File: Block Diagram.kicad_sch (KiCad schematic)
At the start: 0 parts

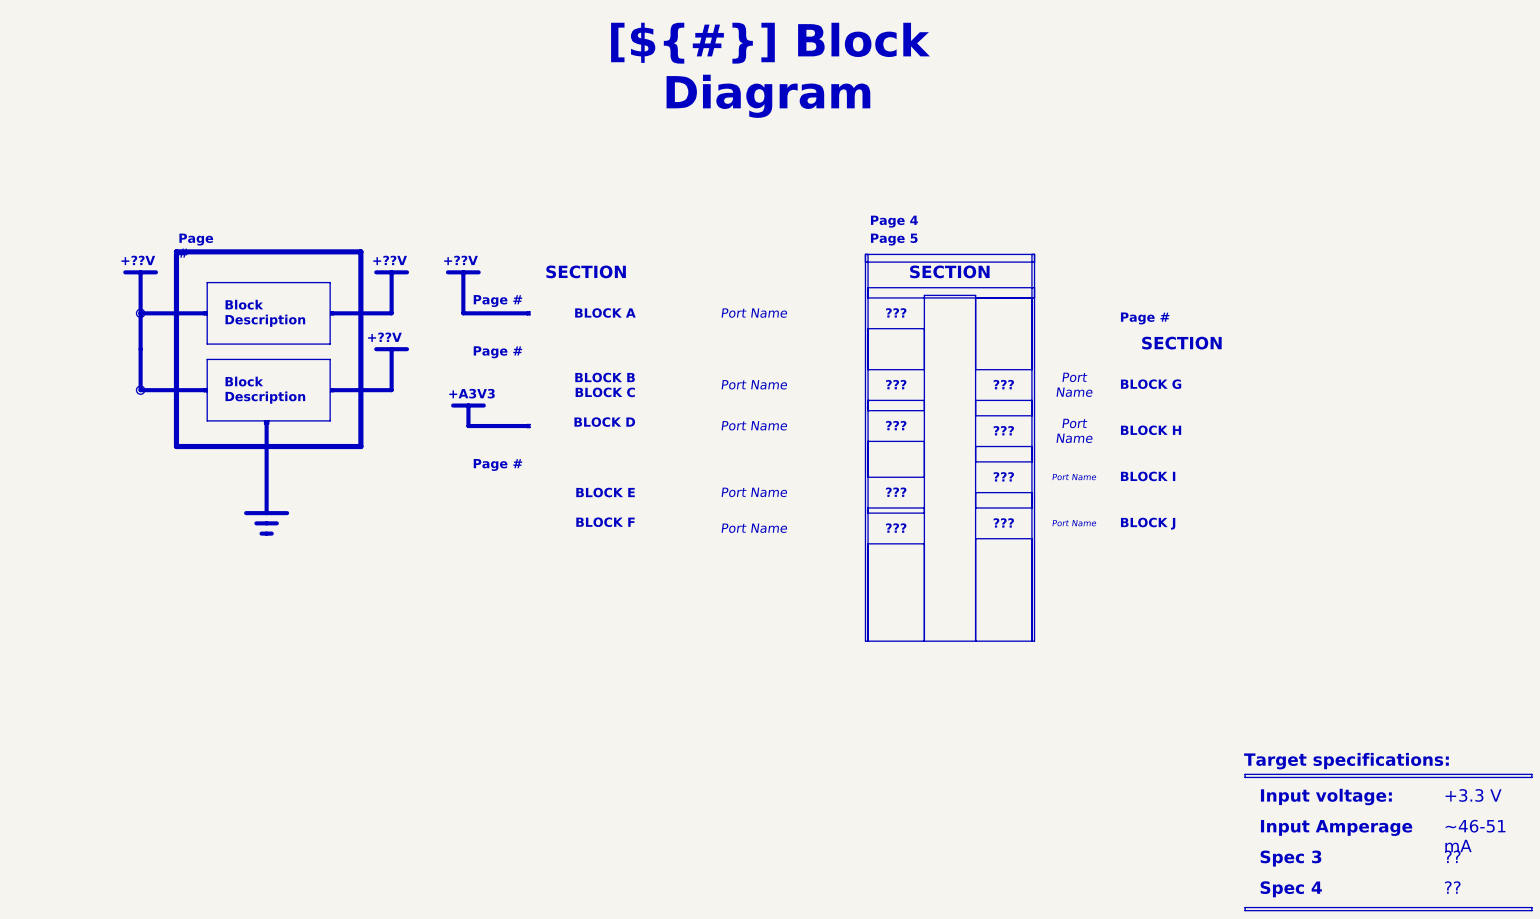
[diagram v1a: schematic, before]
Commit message: Fill template pages: block diagram, power sequencing, notes, revision history
Block Diagram and Power - Sequencing rebuilt from the real design (values computed
from the schematic); cover-page design notes, connector pinout notes, title-block
references; kicad-mcp-pro MCP config (.mcp.json).

Co-Authored-By: Claude Opus 5.5 <noreply@anthropic.com>
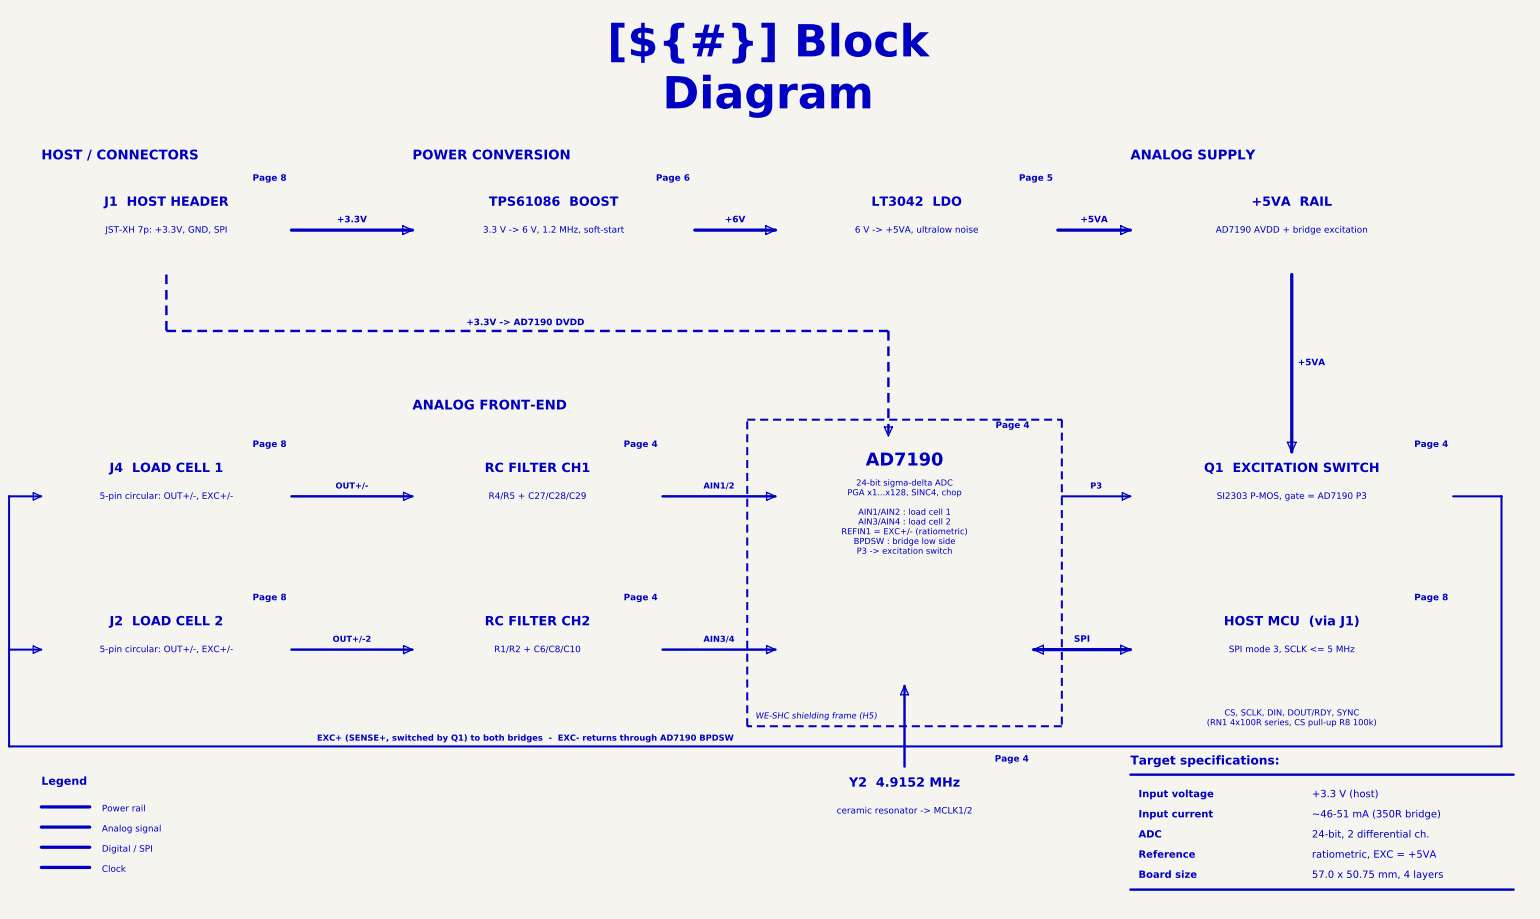
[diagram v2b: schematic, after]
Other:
- note added: "+3.3 V (host)"
- note added: "+3.3V"
- note added: "+3.3V -> AD7190 DVDD"
- note added: "+5VA"
- note added: "+5VA RAIL"
- note added: "+6V"
- note added: "24-bit sigma-delta ADC PGA x1...x128, SINC4, chop AIN1/AIN2 : load cell 1 AIN3/AIN4 : load cell 2 REFIN1 = EXC+/- (ratiometric) BPDSW : bridge low side P3 -> excitation switch"
- note added: "24-bit, 2 differential ch."
- note added: "3.3 V -> 6 V, 1.2 MHz, soft-start"
- note added: "5-pin circular: OUT+/-, EXC+/-"
- note added: "57.0 x 50.75 mm, 4 layers"
- note added: "6 V -> +5VA, ultralow noise"
- note added: "AD7190"
- note added: "AD7190 AVDD + bridge excitation"
- note added: "ADC"
- note added: "AIN1/2"
- note added: "AIN3/4"
- note added: "ANALOG FRONT-END"
- note added: "ANALOG SUPPLY"
- note added: "Analog signal"
- note added: "Board size"
- note added: "CS, SCLK, DIN, DOUT/RDY, SYNC (RN1 4x100R series, CS pull-up R8 100k)"
- note added: "Clock"
- note added: "Digital / SPI"
- note added: "EXC+ (SENSE+, switched by Q1) to both bridges - EXC- returns through AD7190 BPDSW"
- note added: "HOST / CONNECTORS"
- note added: "HOST MCU (via J1)"
- note added: "Input current"
- note added: "Input voltage"
- note added: "J1 HOST HEADER"
- note added: "J2 LOAD CELL 2"
- note added: "J4 LOAD CELL 1"
- note added: "JST-XH 7p: +3.3V, GND, SPI"
- note added: "LT3042 LDO"
- note added: "Legend"
- note added: "OUT+/-"
- note added: "OUT+/-2"
- note added: "P3"
- note added: "POWER CONVERSION"
- note added: "Page 4"
- note added: "Page 5"
- note added: "Page 6"
- note added: "Page 8"
- note added: "Power rail"
- note added: "Q1 EXCITATION SWITCH"
- note added: "R1/R2 + C6/C8/C10"
- note added: "R4/R5 + C27/C28/C29"
- note added: "RC FILTER CH1"
- note added: "RC FILTER CH2"
- note added: "Reference"
- note added: "SI2303 P-MOS, gate = AD7190 P3"
- note added: "SPI"
- note added: "SPI mode 3, SCLK <= 5 MHz"
- note added: "TPS61086 BOOST"
- note added: "Target specifications:"
- note added: "WE-SHC shielding frame (H5)"
- note added: "Y2 4.9152 MHz"
- note added: "ceramic resonator -> MCLK1/2"
- note added: "ratiometric, EXC = +5VA"
- note added: "~46-51 mA (350R bridge)"
- note removed: "+??V"
- note removed: "+A3V3"
